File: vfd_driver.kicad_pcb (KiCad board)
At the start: 2 copper layers, 94 x 58 mm, 44 parts, among them J2 futaba_7_lt_44z, J3 Input, Q1 IRLZ34, Q2 IRF640, Q3 BC817, Q4 BC807, Q5 BC817, Q6 BC807, T1 Transformer_1P_SS, U1 ATTINY13-20PU, U2 74HC595, U3 74HC595, U4 74HC595, U5 TBD62783A, U6 TBD62783A, U7 TBD62783A

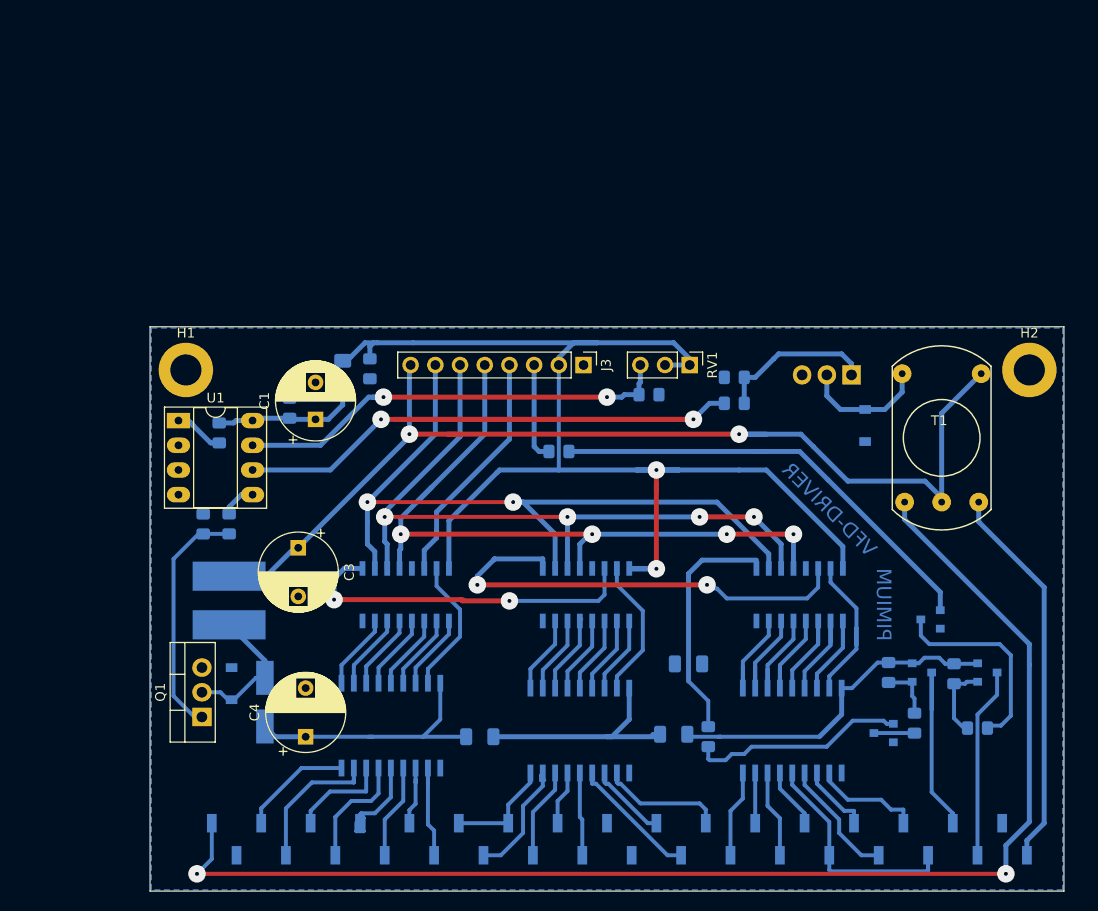
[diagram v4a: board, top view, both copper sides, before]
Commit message: pwr and logic separed
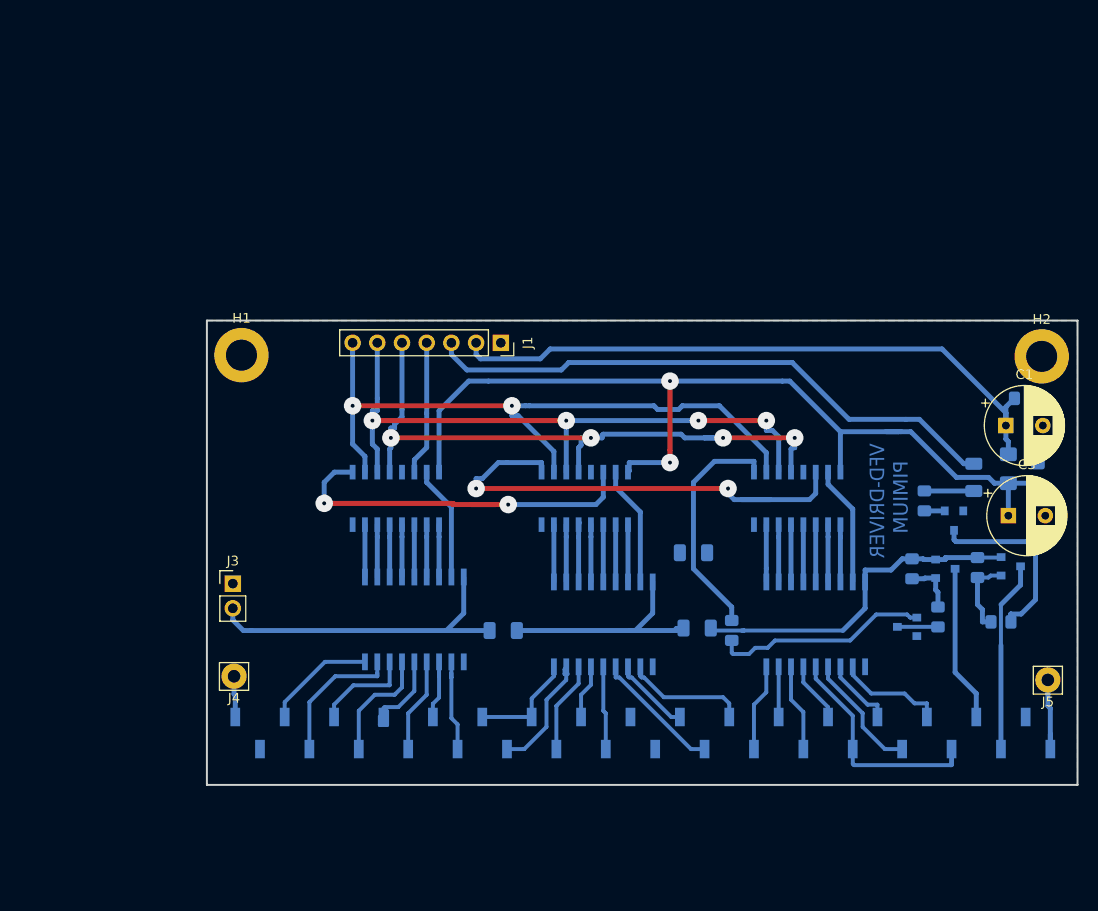
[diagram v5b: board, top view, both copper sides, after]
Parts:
- removed C4: 10u/63v, Capacitor_THT:CP_Radial_D8.0mm_P5.00mm
- removed D1, D3: SD_103BW, Diode_SMD:D_SOD-123
- removed D2: SS14, Diode_SMD:D_SMA_Handsoldering
- removed L1: 330, Choke_SMD:Choke_CD75
- removed Q1: IRLZ34, Package_TO_SOT_THT:TO-220-3_Vertical
- removed Q2: IRF640, Package_TO_SOT_THT:TO-220-3_Vertical
- removed R11: 1K, Resistor_SMD:R_0805_2012Metric_Pad1.15x1.40mm_HandSolder
- removed R15: 10k, Resistor_SMD:R_0805_2012Metric_Pad1.15x1.40mm_HandSolder
- removed R2, R4: 100k, Resistor_SMD:R_0805_2012Metric_Pad1.15x1.40mm_HandSolder
- removed R3: 33, Resistor_SMD:R_0805_2012Metric_Pad1.15x1.40mm_HandSolder
- removed RV1: 10k, Connector_PinHeader_2.54mm:PinHeader_1x03_P2.54mm_Vertical
- removed T1: Transformer_1P_SS, custom_footprint:Transformer_toroid_v_18mm
- removed U1: ATTINY13-20PU, Package_DIP:DIP-8_W7.62mm_Socket_LongPads
- added J1: Input, Connector_PinSocket_2.54mm:PinSocket_1x07_P2.54mm_Vertical, F.Cu at (63.9, 31.2)
- added J4: FIL_n, Connector_Pin:Pin_D1.4mm_L8.5mm_W2.8mm_FlatFork, F.Cu at (36.4, 65.5)
- added J5: FIL_p, Connector_Pin:Pin_D1.4mm_L8.5mm_W2.8mm_FlatFork, F.Cu at (120.1, 65.9)
- C3: value 10u/63v -> 10u; footprint Capacitor_THT:CP_Radial_D8.0mm_P5.00mm -> Capacitor_THT:CP_Radial_D8.0mm_P3.80mm
- J3: value Input -> High Volt; footprint Connector_PinHeader_2.54mm:PinHeader_1x08_P2.54mm_Vertical -> Connector_PinHeader_2.54mm:PinHeader_1x02_P2.54mm_Vertical
- R1: value 33 -> 0; footprint Resistor_SMD:R_0805_2012Metric_Pad1.15x1.40mm_HandSolder -> Resistor_SMD:R_1206_3216Metric
- moved R1 76.7 mm to (112.5, 45.1)
- moved C2 75.6 mm to (117.7, 37.0), turned to 0 degrees
- moved C3 73.1 mm to (116.1, 49.0), turned to 0 degrees
- moved C1 71.0 mm to (115.8, 39.8), turned to 0 degrees
- moved C5 69.5 mm to (119.1, 44.7), turned to 90 degrees
- moved L2 69.1 mm to (116.1, 44.2), turned to 90 degrees
- moved J3 42.5 mm to (36.3, 56.0), turned to 0 degrees
- moved R5 37.9 mm to (107.4, 47.5), turned to 270 degrees
- moved R14 11.4 mm to (83.7, 52.8)
- moved J2 11.2 mm to (78.5, 71.4)
- moved R6 11.2 mm to (112.9, 54.4)
- moved U7 11.2 mm to (96.3, 60.2)
- moved R10 11.2 mm to (108.8, 59.4)
- moved R13 11.2 mm to (84.1, 60.6)
- moved U6 11.2 mm to (74.4, 60.2)
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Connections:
- C3 pad 1: +5V -> VCC
- J2 pad 1: /FIL_n -> Net-(J2-Pad1)
- J2 pad 34: /FIL_p -> Net-(J2-Pad34)
- J3 pad 2: VCC -> +36V
- R1 pad 1: Net-(Q1-Pad1) -> Net-(R1-Pad1)
- R1 pad 2: /HIGH_VOLT -> /GRAD
- R5 pad 1: /GRAD -> Net-(R1-Pad1)
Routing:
- net /FIL_n: track 133.6 -> 0.00 mm, vias 2 -> 0
- net +5V: track 108.8 -> 0.00 mm, vias 2 -> 0
- net /FILAMENT: track 81.7 -> 0.00 mm, vias 2 -> 0
- net VDD: track 15.1 -> 66.5 mm
- net /GRAD: track 10.1 -> 60.2 mm
- net /ADC: track 46.5 -> 0.00 mm, vias 2 -> 0
- net Net-(Q3-Pad1): track 46.9 -> 2.10 mm
- net /FIL_p: track 39.8 -> 0.00 mm
- net VCC: track 133.7 -> 95.0 mm
- net Net-(Q1-Pad1): track 24.7 -> 0.00 mm
- net Net-(Q2-Pad1): track 16.3 -> 0.00 mm
- net Net-(D1-Pad1): track 15.8 -> 0.00 mm
- net Net-(D3-Pad1): track 13.1 -> 0.00 mm
- net /DATA: track 25.9 -> 13.8 mm
- net /nSRCLR: track 78.4 -> 69.2 mm
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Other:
- board size 94 x 58 mm -> 89.5 x 47.8 mm

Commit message: Power and logic are separated and working well.
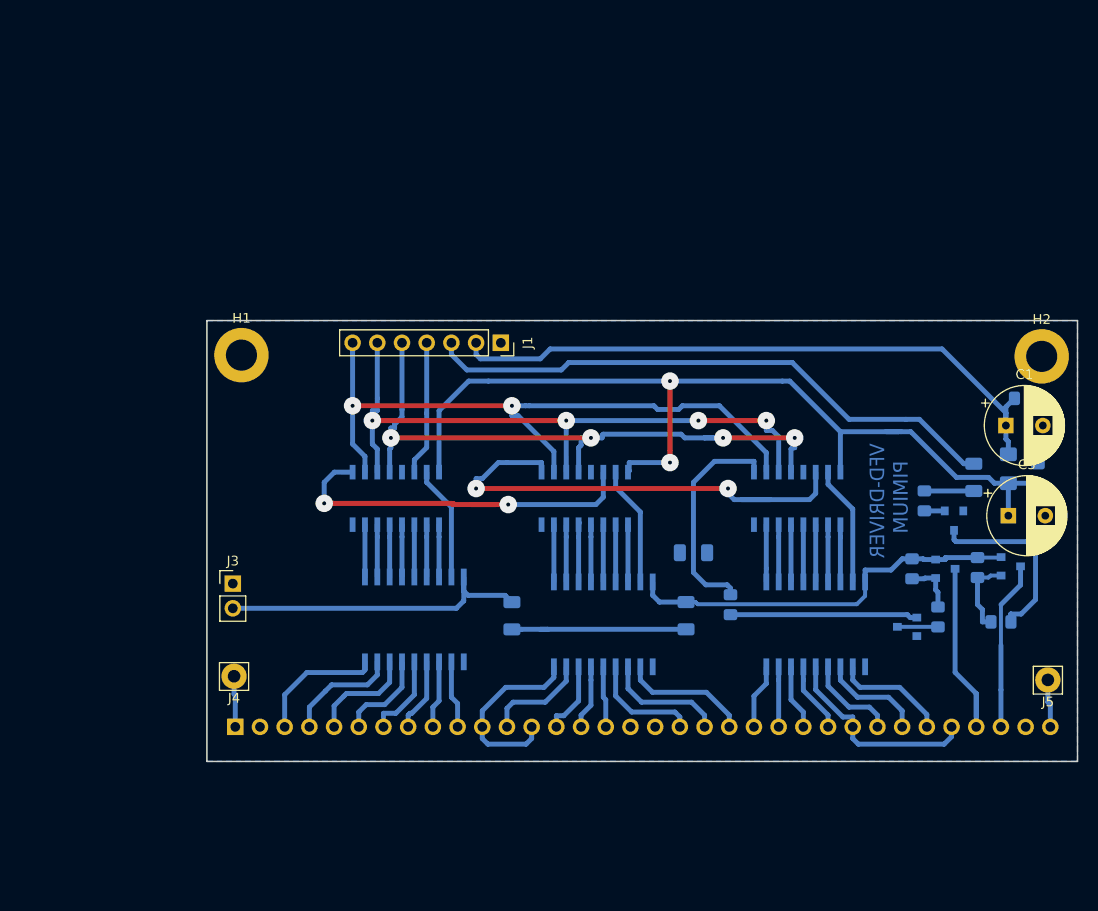
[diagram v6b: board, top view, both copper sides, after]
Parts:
- J2: footprint Connector_PinSocket_2.54mm:PinSocket_1x34_P2.54mm_Vertical_SMD_Pin1Left -> Connector_PinSocket_2.54mm:PinSocket_1x34_P2.54mm_Vertical
- moved J2 41.9 mm to (36.6, 70.7)
- moved R8 2.65 mm to (87.5, 58.2)
- moved R12 1.76 mm to (65.0, 59.3), turned to 90 degrees
- moved R13 1.71 mm to (82.9, 59.3), turned to 90 degrees
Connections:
- net /nSRCLR renamed /~SRCLR
- U6 pad 12: /g -> /G3
- U6 pad 13: /G3 -> /g
- U7 pad 12: /b -> /a
- U7 pad 13: /a -> /b
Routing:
- net +36V: track 110.6 -> 93.4 mm
- net /G5: track 11.2 -> 19.5 mm
- net /G1: track 25.4 -> 21.3 mm
- net Net-(J2-Pad34): track 8.74 -> 4.93 mm
- net /g: track 8.04 -> 11.5 mm
- net /S11: track 16.1 -> 19.6 mm
- net /S8: track 14.7 -> 11.7 mm
- net Net-(Q5-Pad1): track 22.2 -> 19.3 mm
- net /S4: track 9.70 -> 6.95 mm
- net /S3: track 13.2 -> 10.7 mm
- net /S7: track 12.0 -> 9.64 mm
- net /e: track 8.99 -> 6.70 mm
- net /d: track 8.99 -> 6.70 mm
- net /S10: track 19.6 -> 17.3 mm
- net /G4: track 8.57 -> 6.28 mm
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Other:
- board size 89.5 x 47.8 mm -> 89.5 x 45.3 mm

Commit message: Add a 4th shift register and suppress the grad-pin input
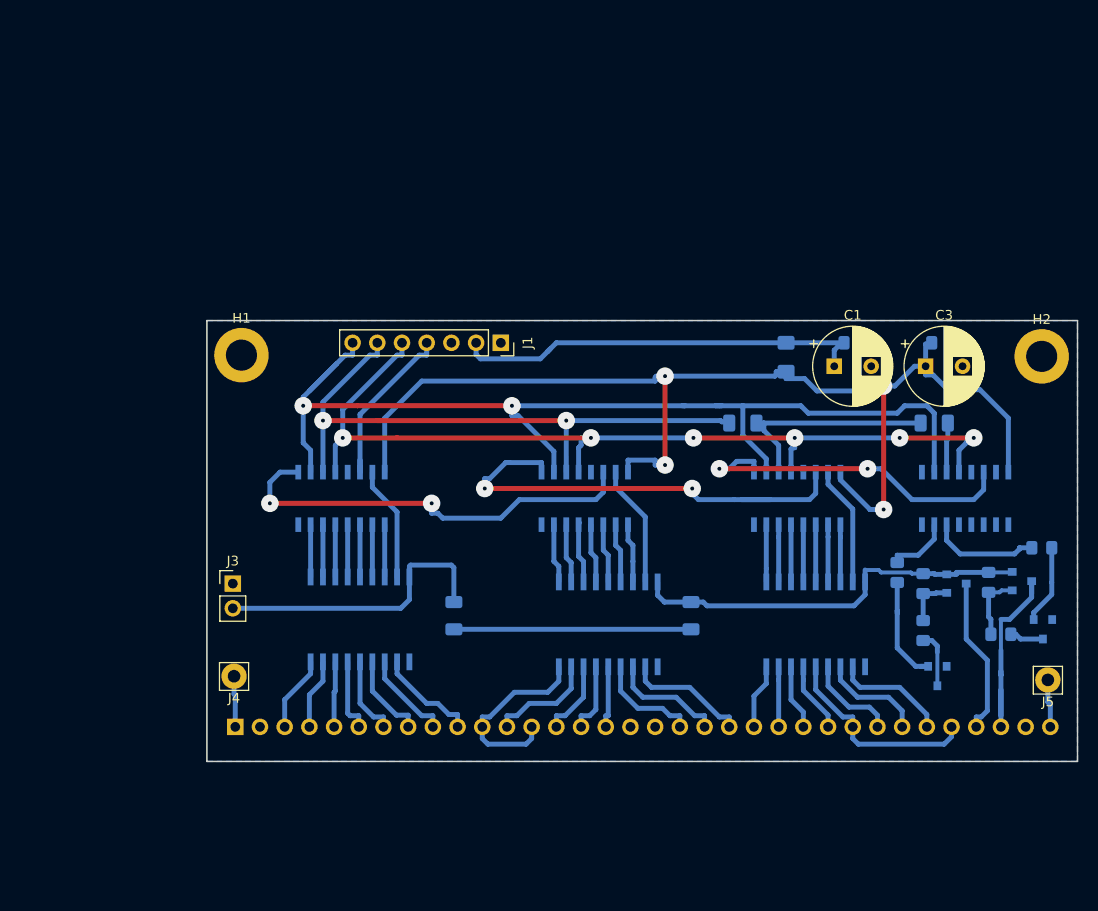
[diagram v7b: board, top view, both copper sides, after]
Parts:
- removed R14: 0, Resistor_SMD:R_1206_3216Metric
- added R2: 0, Resistor_SMD:R_1206_3216Metric, B.Cu at (108.5, 39.5)
- added U1: 74HC595, Package_SO:SOIC-16_3.9x9.9mm_P1.27mm, B.Cu at (111.6, 47.2)
- moved L2 25.6 mm to (93.2, 32.7)
- moved R1 24.4 mm to (88.8, 39.5), turned to 0 degrees
- moved C1 18.7 mm to (98.2, 33.7)
- moved C2 18.4 mm to (100.2, 31.2)
- moved C3 17.6 mm to (107.6, 33.7)
- moved R8 17.5 mm to (104.6, 54.9)
- moved C5 16.7 mm to (109.2, 31.2), turned to 0 degrees
- moved Q3 14.4 mm to (119.6, 60.7)
- moved R5 13.0 mm to (119.5, 52.3), turned to 0 degrees
- moved R12 5.97 mm to (59.1, 59.3)
- moved Q5 5.94 mm to (108.8, 65.5), turned to 270 degrees
- moved U2 5.59 mm to (47.5, 47.2)
- moved U5 5.59 mm to (49.4, 59.7)
- moved R10 2.07 mm to (107.3, 60.8)
- moved Q4 1.91 mm to (117.5, 55.8)
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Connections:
- J1 pad 3: /GRAD -> (no net)
- R1 pad 1: Net-(R1-Pad1) -> /SRCLK
- R1 pad 2: /GRAD -> /SRCLK
- R5 pad 1: Net-(R1-Pad1) -> /Q4G
- R8 pad 1: /Q2 -> /Q4H
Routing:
- net /GRAD: track 60.2 -> 0.00 mm
- net /~SRCLR: track 69.2 -> 109.7 mm
- net /RCLK: track 67.2 -> 94.4 mm, vias 4 -> 6
- net /SRCLK: track 67.4 -> 93.5 mm, vias 4 -> 2
- net VCC: track 95.0 -> 119.9 mm, vias 2 -> 4
- net VDD: track 66.5 -> 43.2 mm
- net Net-(Q3-Pad3): track 19.2 -> 3.51 mm
- net /Q2: track 22.7 -> 35.3 mm, vias 0 -> 2
- net /Q4G: track 0.00 -> 11.3 mm
- net /Q0: track 54.8 -> 45.6 mm
- net Net-(Q5-Pad1): track 19.3 -> 11.7 mm
- net /Q4H: track 0.00 -> 6.74 mm
- net Net-(Q3-Pad1): track 2.10 -> 8.15 mm
- net /S9: track 13.5 -> 7.79 mm
- net Net-(R1-Pad1): track 5.08 -> 0.00 mm
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
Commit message: add a protecting diode to the power input.
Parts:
- added D1: SD103BW, Diode_SMD:D_SOD-123, B.Cu at (70.7, 32.0)
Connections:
- C1 pad 1: VDD -> Net-(C1-Pad1)
- C2 pad 1: VDD -> Net-(C1-Pad1)
- J1 pad 3: (no net) -> GND
- L2 pad 2: VDD -> Net-(C1-Pad1)
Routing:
- net VDD: track 43.2 -> 9.80 mm
- net Net-(C1-Pad1): track 0.00 -> 30.5 mm
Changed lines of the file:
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@@
     (thickness 1.6)
     (drawings 6)
-    (tracks 446)
+    (tracks 450)
     (zones 0)
-    (modules 33)
-    (nets 72)
+    (modules 34)
+    (nets 73)
   )
   (page A4 portrait)
@@
   )
   (setup
-    (last_trace_width 0.25)
+    (last_trace_width 0.508)
     (user_trace_width 0.4064)
     (user_trace_width 0.508)
@@
   (net 70 /Q4G)
   (net 71 /Q4H)
+  (net 72 "Net-(C1-Pad1)")
   (net_class Default "This is the default net class."
     (clearance 0.2)
@@
     (add_net /~SRCLR)
     (add_net GND)
+    (add_net "Net-(C1-Pad1)")
     (add_net "Net-(J2-Pad1)")
     (add_net "Net-(J2-Pad34)")
@@
     (uvia_dia 0.3)
     (uvia_drill 0.1)
+  )
+  (module Diode_SMD:D_SOD-123 (layer B.Cu)
+    (at 70.739 32.004 180)
+    (descr SOD-123)
+    (tags SOD-123)
+    (attr smd)
+    (fp_text reference D1 (at 0 2 180) (layer B.SilkS)
+      (effects (font (size 1 1) (thickness 0.15)) (justify mirror))
+    )
+    (fp_text value SD103BW (at 0 -2.1 180) (layer B.Fab)
+      (effects (font (size 1 1) (thickness 0.15)) (justify mirror))
+    )
+    (fp_text user %R (at 0 2 180) (layer B.Fab)
+      (effects (font (size 1 1) (thickness 0.15)) (justify mirror))
+    )
+    (fp_line (start -2.25 1) (end -2.25 -1) (layer B.SilkS) (width 0.12))
+    (fp_line (start 0.25 0) (end 0.75 0) (layer B.Fab) (width 0.1))
+    (fp_line (start 0.25 -0.4) (end -0.35 0) (layer B.Fab) (width 0.1))
+    (fp_line (start 0.25 0.4) (end 0.25 -0.4) (layer B.Fab) (width 0.1))
+    (fp_line (start -0.35 0) (end 0.25 0.4) (layer B.Fab) (width 0.1))
+    (fp_line (start -0.35 0) (end -0.35 -0.55) (layer B.Fab) (width 0.1))
+    (fp_line (start -0.35 0) (end -0.35 0.55) (layer B.Fab) (width 0.1))
+    (fp_line (start -0.75 0) (end -0.35 0) (layer B.Fab) (width 0.1))
+    (fp_line (start -1.4 -0.9) (end -1.4 0.9) (layer B.Fab) (width 0.1))
+    (fp_line (start 1.4 -0.9) (end -1.4 -0.9) (layer B.Fab) (width 0.1))
+    (fp_line (start 1.4 0.9) (end 1.4 -0.9) (layer B.Fab) (width 0.1))
+    (fp_line (start -1.4 0.9) (end 1.4 0.9) (layer B.Fab) (width 0.1))
+    (fp_line (start -2.35 1.15) (end 2.35 1.15) (layer B.CrtYd) (width 0.05))
+    (fp_line (start 2.35 1.15) (end 2.35 -1.15) (layer B.CrtYd) (width 0.05))
+    (fp_line (start 2.35 -1.15) (end -2.35 -1.15) (layer B.CrtYd) (width 0.05))
+    (fp_line (start -2.35 1.15) (end -2.35 -1.15) (layer B.CrtYd) (width 0.05))
+    (fp_line (start -2.25 -1) (end 1.65 -1) (layer B.SilkS) (width 0.12))
+    (fp_line (start -2.25 1) (end 1.65 1) (layer B.SilkS) (width 0.12))
+    (pad 1 smd rect (at -1.65 0 180) (size 0.9 1.2) (layers B.Cu B.Paste B.Mask)
+      (net 72 "Net-(C1-Pad1)"))
+    (pad 2 smd rect (at 1.65 0 180) (size 0.9 1.2) (layers B.Cu B.Paste B.Mask)
+      (net 66 VDD))
+    (model ${KISYS3DMOD}/Diode_SMD.3dshapes/D_SOD-123.wrl
+      (at (xyz 0 0 0))
+      (scale (xyz 1 1 1))
+      (rotate (xyz 0 0 0))
+    )
   )
   (module Capacitor_THT:CP_Radial_D8.0mm_P3.80mm (layer F.Cu)
@@
     )
     (pad 1 thru_hole rect (at 0 0) (size 1.6 1.6) (drill 0.8) (layers *.Cu *.Mask)
-      (net 66 VDD))
+      (net 72 "Net-(C1-Pad1)"))
     (pad 2 thru_hole circle (at 3.8 0) (size 1.6 1.6) (drill 0.8) (layers *.Cu *.Mask)
       (net 1 GND))
@@
     )
     (pad 1 smd roundrect (at -1.025 0) (size 1.15 1.4) (layers B.Cu B.Paste B.Mask) (roundrect_rratio 0.217391)
-      (net 66 VDD))
+      (net 72 "Net-(C1-Pad1)"))
     (pad 2 smd roundrect (at 1.025 0) (size 1.15 1.4) (layers B.Cu B.Paste B.Mask) (roundrect_rratio 0.217391)
       (net 1 GND))
@@
       (net 2 VCC))
     (pad 2 smd roundrect (at 1.4875 0 90) (size 1.425 1.75) (layers B.Cu B.Paste B.Mask) (roundrect_rratio 0.175439)
-      (net 66 VDD))
+      (net 72 "Net-(C1-Pad1)"))
     (model ${KISYS3DMOD}/Inductor_SMD.3dshapes/L_1206_3216Metric.wrl
       (at (xyz 0 0 0))
@@
     (pad 2 thru_hole oval (at 0 2.54 270) (size 1.7 1.7) (drill 1) (layers *.Cu *.Mask)
       (net 66 VDD))
-    (pad 3 thru_hole oval (at 0 5.08 270) (size 1.7 1.7) (drill 1) (layers *.Cu *.Mask))
+    (pad 3 thru_hole oval (at 0 5.08 270) (size 1.7 1.7) (drill 1) (layers *.Cu *.Mask)
+      (net 1 GND))
     (pad 4 thru_hole oval (at 0 7.62 270) (size 1.7 1.7) (drill 1) (layers *.Cu *.Mask)
       (net 31 /DATA))
@@
   (segment (start 61.341 32.444081) (end 61.789919 32.893) (width 0.508) (layer B.Cu) (net 66))
   (segment (start 61.789919 32.893) (end 67.945 32.893) (width 0.508) (layer B.Cu) (net 66))
-  (segment (start 98.171 33.655) (end 98.171 32.004) (width 0.508) (layer B.Cu) (net 66) (status 10))
-  (segment (start 98.933 31.242) (end 99.178 31.242) (width 0.508) (layer B.Cu) (net 66) (status 30))
-  (segment (start 98.171 32.004) (end 98.933 31.242) (width 0.508) (layer B.Cu) (net 66) (status 20))
-  (segment (start 69.596 31.242) (end 68.707 32.131) (width 0.508) (layer B.Cu) (net 66))
-  (segment (start 99.178 31.242) (end 69.596 31.242) (width 0.508) (layer B.Cu) (net 66) (status 10))
-  (segment (start 68.707 32.131) (end 68.961 31.877) (width 0.508) (layer B.Cu) (net 66))
-  (segment (start 67.945 32.893) (end 68.707 32.131) (width 0.508) (layer B.Cu) (net 66))
+  (segment (start 69.089 32.004) (end 68.326 32.004) (width 0.508) (layer B.Cu) (net 66))
+  (segment (start 68.326 32.512) (end 67.945 32.893) (width 0.508) (layer B.Cu) (net 66))
+  (segment (start 68.326 32.004) (end 68.326 32.512) (width 0.508) (layer B.Cu) (net 66))
+  (segment (start 98.171 33.655) (end 98.171 32.004) (width 0.508) (layer B.Cu) (net 72) (status 10))
+  (segment (start 98.933 31.242) (end 99.178 31.242) (width 0.508) (layer B.Cu) (net 72) (status 30))
+  (segment (start 98.171 32.004) (end 98.933 31.242) (width 0.508) (layer B.Cu) (net 72) (status 20))
   (segment (start 36.449 67.370477) (end 36.576 67.497477) (width 0.508) (layer B.Cu) (net 67))
   (segment (start 36.449 65.532) (end 36.449 67.370477) (width 0.508) (layer B.Cu) (net 67) (status 10))
@@
   (segment (start 104.648 53.086) (end 106.807 53.086) (width 0.508) (layer B.Cu) (net 71))
   (segment (start 104.648 53.839) (end 104.648 53.086) (width 0.508) (layer B.Cu) (net 71))
+  (segment (start 93.091 31.369) (end 93.218 31.242) (width 0.508) (layer B.Cu) (net 72))
+  (segment (start 73.152 32.004) (end 73.152 31.369) (width 0.508) (layer B.Cu) (net 72))
+  (segment (start 73.152 31.369) (end 93.091 31.369) (width 0.508) (layer B.Cu) (net 72))
+  (segment (start 72.389 32.004) (end 73.152 32.004) (width 0.508) (layer B.Cu) (net 72))
+  (segment (start 93.218 31.242) (end 99.178 31.242) (width 0.508) (layer B.Cu) (net 72))
   (zone (net 1) (net_name GND) (layer B.Cu) (hatch edge 0.508)
     (connect_pads (clearance 0.508))
